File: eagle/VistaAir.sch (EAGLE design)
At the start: 11 parts

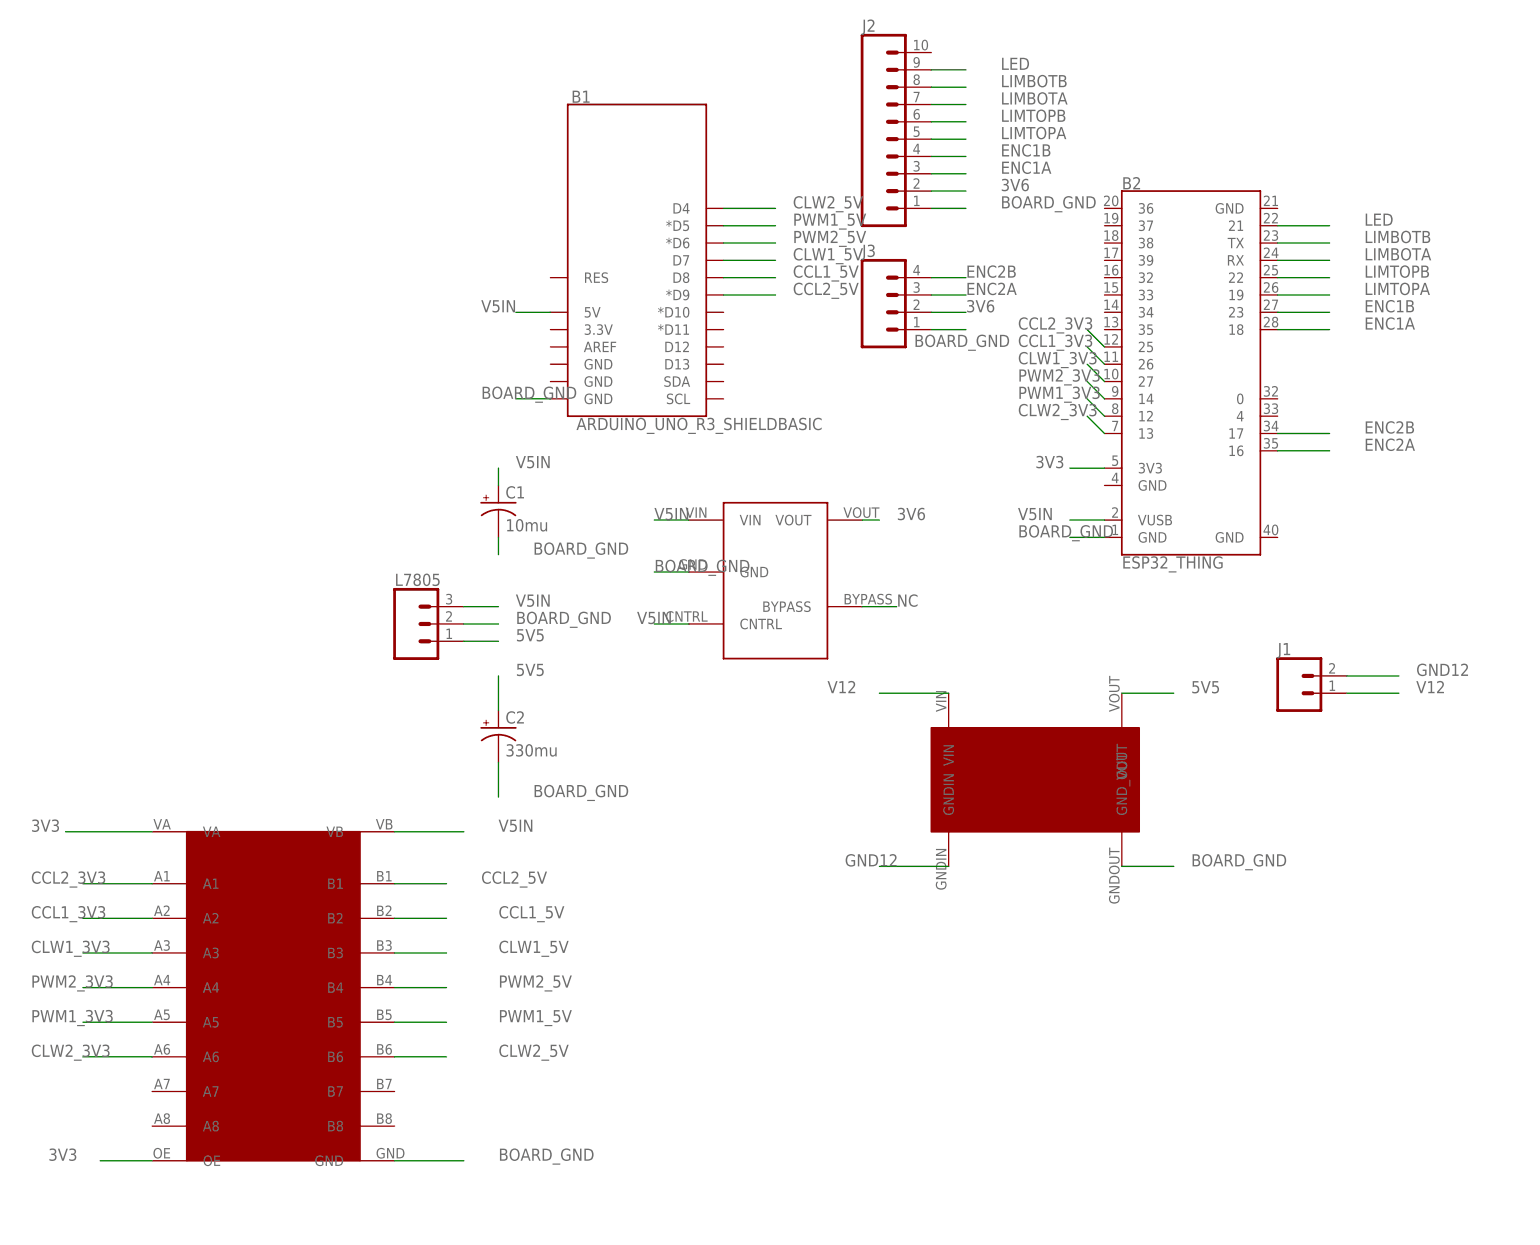
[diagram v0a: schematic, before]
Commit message: still trying to get single power board to work with logic shifter - still failing
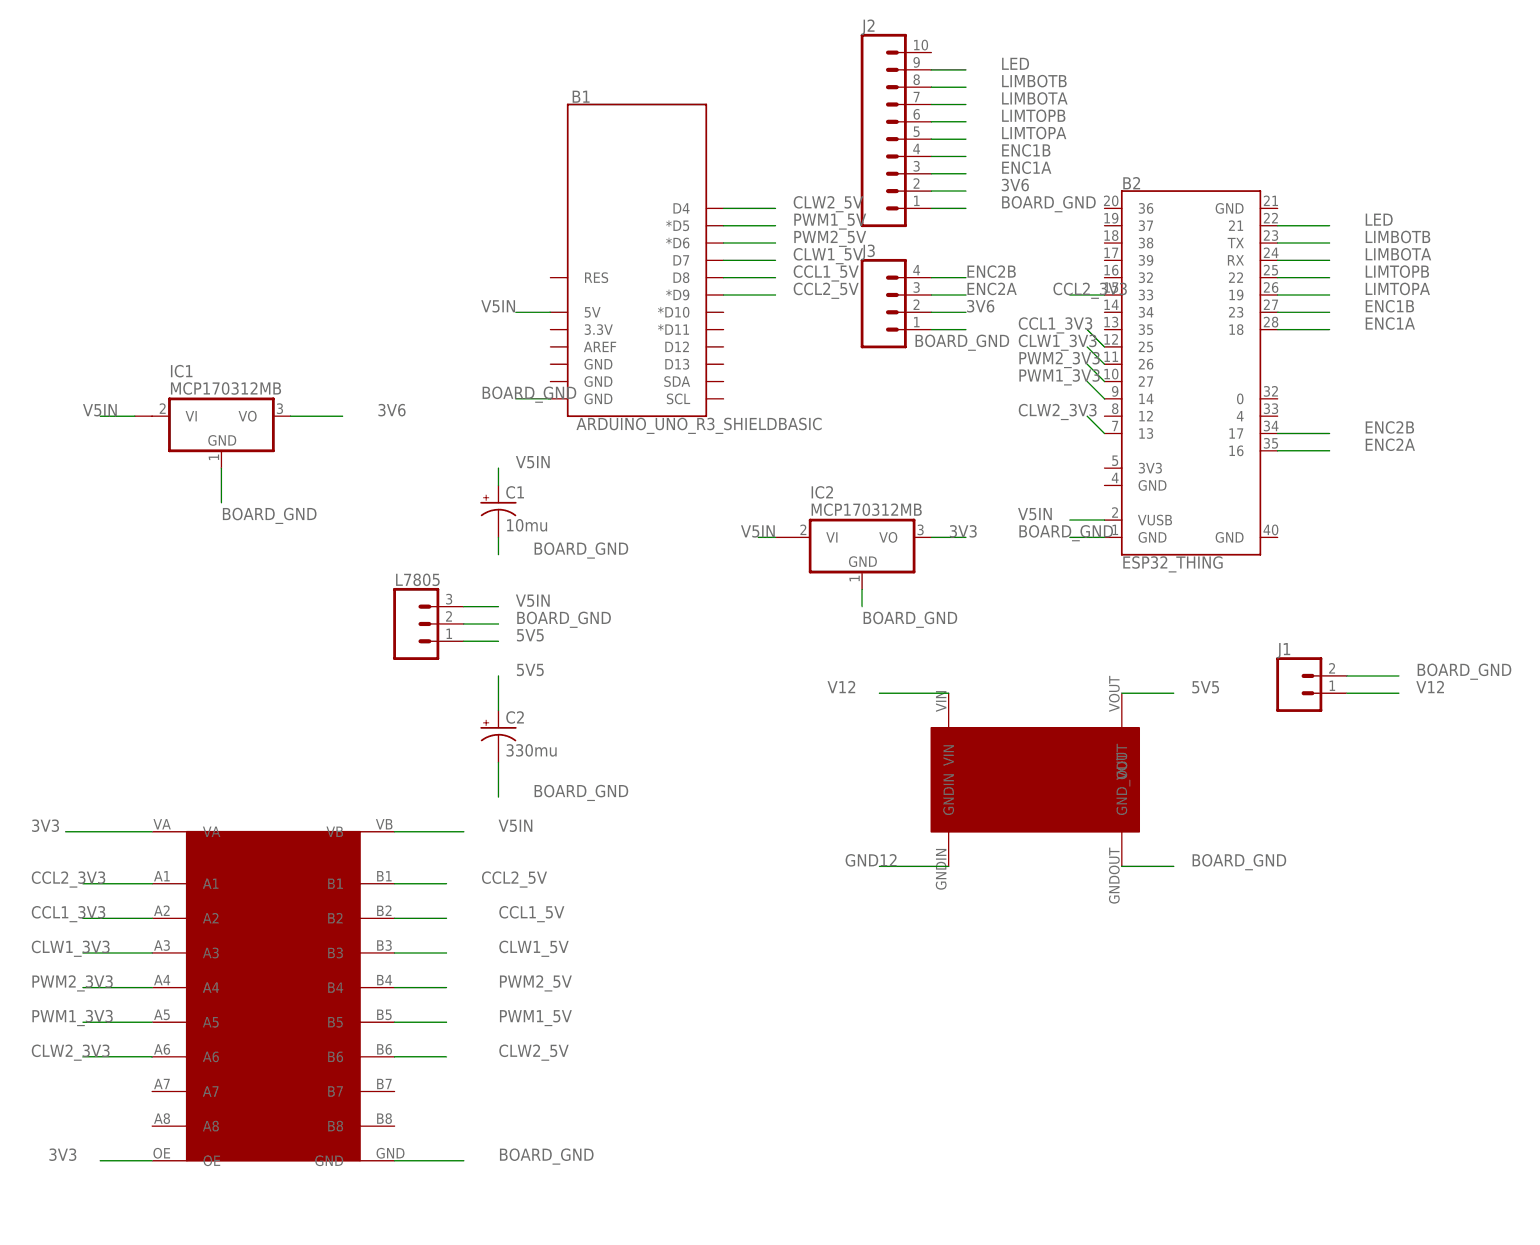
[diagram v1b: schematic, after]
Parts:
- removed U$1: LDO_REGULATOR_LP2985-N, kevins_parts:LDO_REGULATOR_LP2985-N
- added IC1, IC2: MCP170312MB, linear:MCP170312MB
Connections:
- removed net NC: U$1.BYPASS
- net 3V3: now also IC2.VO; no longer B2.3V3@5
- net 3V6: now also IC1.VO; no longer U$1.VOUT
- net BOARD_GND: now also IC1.GND, IC2.GND, J1.2; no longer U$1.GND
- net CCL1_3V3: now also B2.25; no longer B2.26
- net CCL2_3V3: now also B2.33; no longer B2.25
- net CLW1_3V3: now also B2.26; no longer B2.27
- net GND12: no longer J1.2
- net PWM1_3V3: now also B2.14; no longer B2.12
- net PWM2_3V3: now also B2.27; no longer B2.14
- net V5IN: now also IC1.VI1, IC2.VI1; no longer U$1.CNTRL, U$1.VIN
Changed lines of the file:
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@@
 <part name="C1" library="adafruit" deviceset="CPOL-US" device="TT2D5" value="10mu"/>
 <part name="U$2" library="kevins_parts" deviceset="LM2596_STEPDOWN_MODULE" device=""/>
-<part name="U$1" library="kevins_parts" deviceset="LDO_REGULATOR_LP2985-N" device=""/>
 <part name="U$3" library="kevins_parts" deviceset="8_CHANNEL_LOGIC_CONVERTER" device=""/>
+<part name="IC1" library="linear" deviceset="MCP1703*" device="MB" technology="12"/>
+<part name="IC2" library="linear" deviceset="MCP1703*" device="MB" technology="12"/>
 </parts>
 <sheets>
@@
 <instance part="C1" gate="G$1" x="25.4" y="40.64"/>
 <instance part="U$2" gate="G$1" x="99.06" y="-27.94" rot="R270"/>
-<instance part="U$1" gate="G$1" x="83.82" y="30.48"/>
 <instance part="U$3" gate="G$1" x="5.08" y="-35.56"/>
+<instance part="IC1" gate="G$1" x="-15.24" y="53.34"/>
+<instance part="IC2" gate="G$1" x="78.74" y="35.56"/>
 </instances>
 <busses>
@@
 <net name="CLW1_3V3" class="0">
 <segment>
+<pinref part="U$3" gate="G$1" pin="A3"/>
+<wire x1="-25.4" y1="-25.4" x2="-35.56" y2="-25.4" width="0.1524" layer="91"/>
+<label x="-43.18" y="-25.4" size="1.778" layer="95"/>
+</segment>
+<segment>
+<wire x1="114.3" y1="60.96" x2="111.76" y2="63.5" width="0.1524" layer="91"/>
+<label x="101.6" y="63.5" size="1.778" layer="95"/>
+<pinref part="B2" gate="G$1" pin="26"/>
+</segment>
+</net>
+<net name="PWM2_3V3" class="0">
+<segment>
+<pinref part="U$3" gate="G$1" pin="A4"/>
+<wire x1="-25.4" y1="-30.48" x2="-35.56" y2="-30.48" width="0.1524" layer="91"/>
+<label x="-43.18" y="-30.48" size="1.778" layer="95"/>
+</segment>
+<segment>
 <wire x1="114.3" y1="58.42" x2="111.76" y2="60.96" width="0.1524" layer="91"/>
 <label x="101.6" y="60.96" size="1.778" layer="95"/>
 <pinref part="B2" gate="G$1" pin="27"/>
 </segment>
-<segment>
-<pinref part="U$3" gate="G$1" pin="A3"/>
-<wire x1="-25.4" y1="-25.4" x2="-35.56" y2="-25.4" width="0.1524" layer="91"/>
-<label x="-43.18" y="-25.4" size="1.778" layer="95"/>
-</segment>
-</net>
-<net name="PWM2_3V3" class="0">
+</net>
+<net name="PWM1_3V3" class="0">
+<segment>
+<pinref part="U$3" gate="G$1" pin="A5"/>
+<wire x1="-25.4" y1="-35.56" x2="-35.56" y2="-35.56" width="0.1524" layer="91"/>
+<label x="-43.18" y="-35.56" size="1.778" layer="95"/>
+</segment>
 <segment>
 <wire x1="114.3" y1="55.88" x2="111.76" y2="58.42" width="0.1524" layer="91"/>
@@
 <pinref part="B2" gate="G$1" pin="14"/>
 </segment>
-<segment>
-<pinref part="U$3" gate="G$1" pin="A4"/>
-<wire x1="-25.4" y1="-30.48" x2="-35.56" y2="-30.48" width="0.1524" layer="91"/>
-<label x="-43.18" y="-30.48" size="1.778" layer="95"/>
-</segment>
-</net>
-<net name="PWM1_3V3" class="0">
-<segment>
-<wire x1="114.3" y1="53.34" x2="111.76" y2="55.88" width="0.1524" layer="91"/>
-<label x="101.6" y="55.88" size="1.778" layer="95"/>
-<pinref part="B2" gate="G$1" pin="12"/>
-</segment>
-<segment>
-<pinref part="U$3" gate="G$1" pin="A5"/>
-<wire x1="-25.4" y1="-35.56" x2="-35.56" y2="-35.56" width="0.1524" layer="91"/>
-<label x="-43.18" y="-35.56" size="1.778" layer="95"/>
-</segment>
 </net>
 <net name="CLW2_3V3" class="0">
@@
 <net name="CCL1_3V3" class="0">
 <segment>
-<wire x1="114.3" y1="60.96" x2="111.76" y2="63.5" width="0.1524" layer="91"/>
-<label x="101.6" y="63.5" size="1.778" layer="95"/>
-<pinref part="B2" gate="G$1" pin="26"/>
-</segment>
-<segment>
 <pinref part="U$3" gate="G$1" pin="A2"/>
 <wire x1="-25.4" y1="-20.32" x2="-35.56" y2="-20.32" width="0.1524" layer="91"/>
 <label x="-43.18" y="-20.32" size="1.778" layer="95"/>
 </segment>
-</net>
-<net name="CCL2_3V3" class="0">
 <segment>
 <wire x1="114.3" y1="63.5" x2="111.76" y2="66.04" width="0.1524" layer="91"/>
@@
 <pinref part="B2" gate="G$1" pin="25"/>
 </segment>
+</net>
+<net name="CCL2_3V3" class="0">
 <segment>
 <pinref part="U$3" gate="G$1" pin="A1"/>
@@
 <label x="-43.18" y="-15.24" size="1.778" layer="95"/>
 </segment>
+<segment>
+<pinref part="B2" gate="G$1" pin="33"/>
+<wire x1="114.3" y1="71.12" x2="109.22" y2="71.12" width="0.1524" layer="91"/>
+<label x="106.68" y="71.12" size="1.778" layer="95"/>
+</segment>
 </net>
 <net name="BOARD_GND" class="1">
@@
 </segment>
 <segment>
-<pinref part="U$1" gate="G$1" pin="GND"/>
-<wire x1="53.34" y1="30.48" x2="48.26" y2="30.48" width="0.1524" layer="91"/>
-<label x="48.26" y="30.48" size="1.778" layer="95"/>
-</segment>
-<segment>
 <pinref part="B1" gate="G$1" pin="GND@0"/>
 <wire x1="33.02" y1="55.88" x2="27.94" y2="55.88" width="0.1524" layer="91"/>
@@
 <label x="25.4" y="-55.88" size="1.778" layer="95"/>
 </segment>
+<segment>
+<pinref part="IC1" gate="G$1" pin="GND"/>
+<wire x1="-15.24" y1="45.72" x2="-15.24" y2="40.64" width="0.1524" layer="91"/>
+<label x="-15.24" y="38.1" size="1.778" layer="95"/>
+</segment>
+<segment>
+<pinref part="IC2" gate="G$1" pin="GND"/>
+<wire x1="78.74" y1="27.94" x2="78.74" y2="25.4" width="0.1524" layer="91"/>
+<label x="78.74" y="22.86" size="1.778" layer="95"/>
+</segment>
+<segment>
+<pinref part="J1" gate="G$1" pin="2"/>
+<wire x1="149.86" y1="15.24" x2="157.48" y2="15.24" width="0.1524" layer="91"/>
+<label x="160.02" y="15.24" size="1.778" layer="95"/>
+</segment>
 </net>
 <net name="ENC2B" class="0">
@@
 <net name="V5IN" class="1">
 <segment>
+<pinref part="B1" gate="G$1" pin="5V"/>
+<wire x1="33.02" y1="68.58" x2="27.94" y2="68.58" width="0.1524" layer="91"/>
+<label x="22.86" y="68.58" size="1.778" layer="95"/>
+</segment>
+<segment>
+<pinref part="C1" gate="G$1" pin="+"/>
+<wire x1="25.4" y1="43.18" x2="25.4" y2="45.72" width="0.1524" layer="91"/>
+<label x="27.94" y="45.72" size="1.778" layer="95"/>
+</segment>
+<segment>
+<pinref part="L7805" gate="J$1" pin="3"/>
+<wire x1="20.32" y1="25.4" x2="25.4" y2="25.4" width="0.1524" layer="91"/>
+<label x="27.94" y="25.4" size="1.778" layer="95"/>
+</segment>
+<segment>
+<pinref part="U$3" gate="G$1" pin="VB"/>
+<wire x1="10.16" y1="-7.62" x2="20.32" y2="-7.62" width="0.1524" layer="91"/>
+<label x="25.4" y="-7.62" size="1.778" layer="95"/>
+</segment>
+<segment>
+<pinref part="IC1" gate="G$1" pin="VI1"/>
+<wire x1="-27.94" y1="53.34" x2="-33.02" y2="53.34" width="0.1524" layer="91"/>
+<label x="-35.56" y="53.34" size="1.778" layer="95"/>
+</segment>
+<segment>
+<pinref part="IC2" gate="G$1" pin="VI1"/>
+<wire x1="66.04" y1="35.56" x2="63.5" y2="35.56" width="0.1524" layer="91"/>
+<label x="60.96" y="35.56" size="1.778" layer="95"/>
+</segment>
+<segment>
 <wire x1="114.3" y1="38.1" x2="109.22" y2="38.1" width="0.1524" layer="91"/>
 <label x="101.6" y="38.1" size="1.778" layer="95"/>
 <pinref part="B2" gate="G$1" pin="VUSB@2"/>
 </segment>
-<segment>
-<pinref part="B1" gate="G$1" pin="5V"/>
-<wire x1="33.02" y1="68.58" x2="27.94" y2="68.58" width="0.1524" layer="91"/>
-<label x="22.86" y="68.58" size="1.778" layer="95"/>
-</segment>
-<segment>
-<pinref part="C1" gate="G$1" pin="+"/>
-<wire x1="25.4" y1="43.18" x2="25.4" y2="45.72" width="0.1524" layer="91"/>
-<label x="27.94" y="45.72" size="1.778" layer="95"/>
-</segment>
-<segment>
-<pinref part="L7805" gate="J$1" pin="3"/>
-<wire x1="20.32" y1="25.4" x2="25.4" y2="25.4" width="0.1524" layer="91"/>
-<label x="27.94" y="25.4" size="1.778" layer="95"/>
-</segment>
-<segment>
-<pinref part="U$1" gate="G$1" pin="VIN"/>
-<wire x1="53.34" y1="38.1" x2="48.26" y2="38.1" width="0.1524" layer="91"/>
-<label x="48.26" y="38.1" size="1.778" layer="95"/>
-</segment>
-<segment>
-<pinref part="U$1" gate="G$1" pin="CNTRL"/>
-<wire x1="53.34" y1="22.86" x2="48.26" y2="22.86" width="0.1524" layer="91"/>
-<label x="45.72" y="22.86" size="1.778" layer="95"/>
-</segment>
-<segment>
-<pinref part="U$3" gate="G$1" pin="VB"/>
-<wire x1="10.16" y1="-7.62" x2="20.32" y2="-7.62" width="0.1524" layer="91"/>
-<label x="25.4" y="-7.62" size="1.778" layer="95"/>
-</segment>
 </net>
 <net name="LIMTOPA" class="0">
@@
 <net name="GND12" class="1">
 <segment>
-<pinref part="J1" gate="G$1" pin="2"/>
-<wire x1="149.86" y1="15.24" x2="157.48" y2="15.24" width="0.1524" layer="91"/>
-<label x="160.02" y="15.24" size="1.778" layer="95"/>
-</segment>
-<segment>
 <pinref part="U$2" gate="G$1" pin="GNDIN"/>
 <wire x1="91.44" y1="-12.7" x2="81.28" y2="-12.7" width="0.1524" layer="91"/>
@@
 </segment>
 <segment>
-<pinref part="U$1" gate="G$1" pin="VOUT"/>
-<wire x1="78.74" y1="38.1" x2="81.28" y2="38.1" width="0.1524" layer="91"/>
-<label x="83.82" y="38.1" size="1.778" layer="95"/>
+<pinref part="IC1" gate="G$1" pin="VO"/>
+<wire x1="-5.08" y1="53.34" x2="2.54" y2="53.34" width="0.1524" layer="91"/>
+<label x="7.62" y="53.34" size="1.778" layer="95"/>
 </segment>
 </net>
@@
 </segment>
 </net>
-<net name="NC" class="0">
-<segment>
-<pinref part="U$1" gate="G$1" pin="BYPASS"/>
-<wire x1="78.74" y1="25.4" x2="83.82" y2="25.4" width="0.1524" layer="91"/>
-<label x="83.82" y="25.4" size="1.778" layer="95"/>
-</segment>
-</net>
 <net name="3V3" class="0">
-<segment>
-<pinref part="B2" gate="G$1" pin="3V3@5"/>
-<wire x1="114.3" y1="45.72" x2="109.22" y2="45.72" width="0.1524" layer="91"/>
-<label x="104.14" y="45.72" size="1.778" layer="95"/>
-</segment>
 <segment>
 <pinref part="U$3" gate="G$1" pin="VA"/>
@@
 <label x="-40.64" y="-55.88" size="1.778" layer="95"/>
 </segment>
-</net>
+<segment>
+<pinref part="IC2" gate="G$1" pin="VO"/>
+<wire x1="88.9" y1="35.56" x2="93.98" y2="35.56" width="0.1524" layer="91"/>
+<label x="91.44" y="35.56" size="1.778" layer="95"/>
+</segment>
+</net>

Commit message: barrel jack for board, fix pin numbers for arduino motor test and simplify board - diodes seem to be surplus to requirements. Logic shifting issue is something else
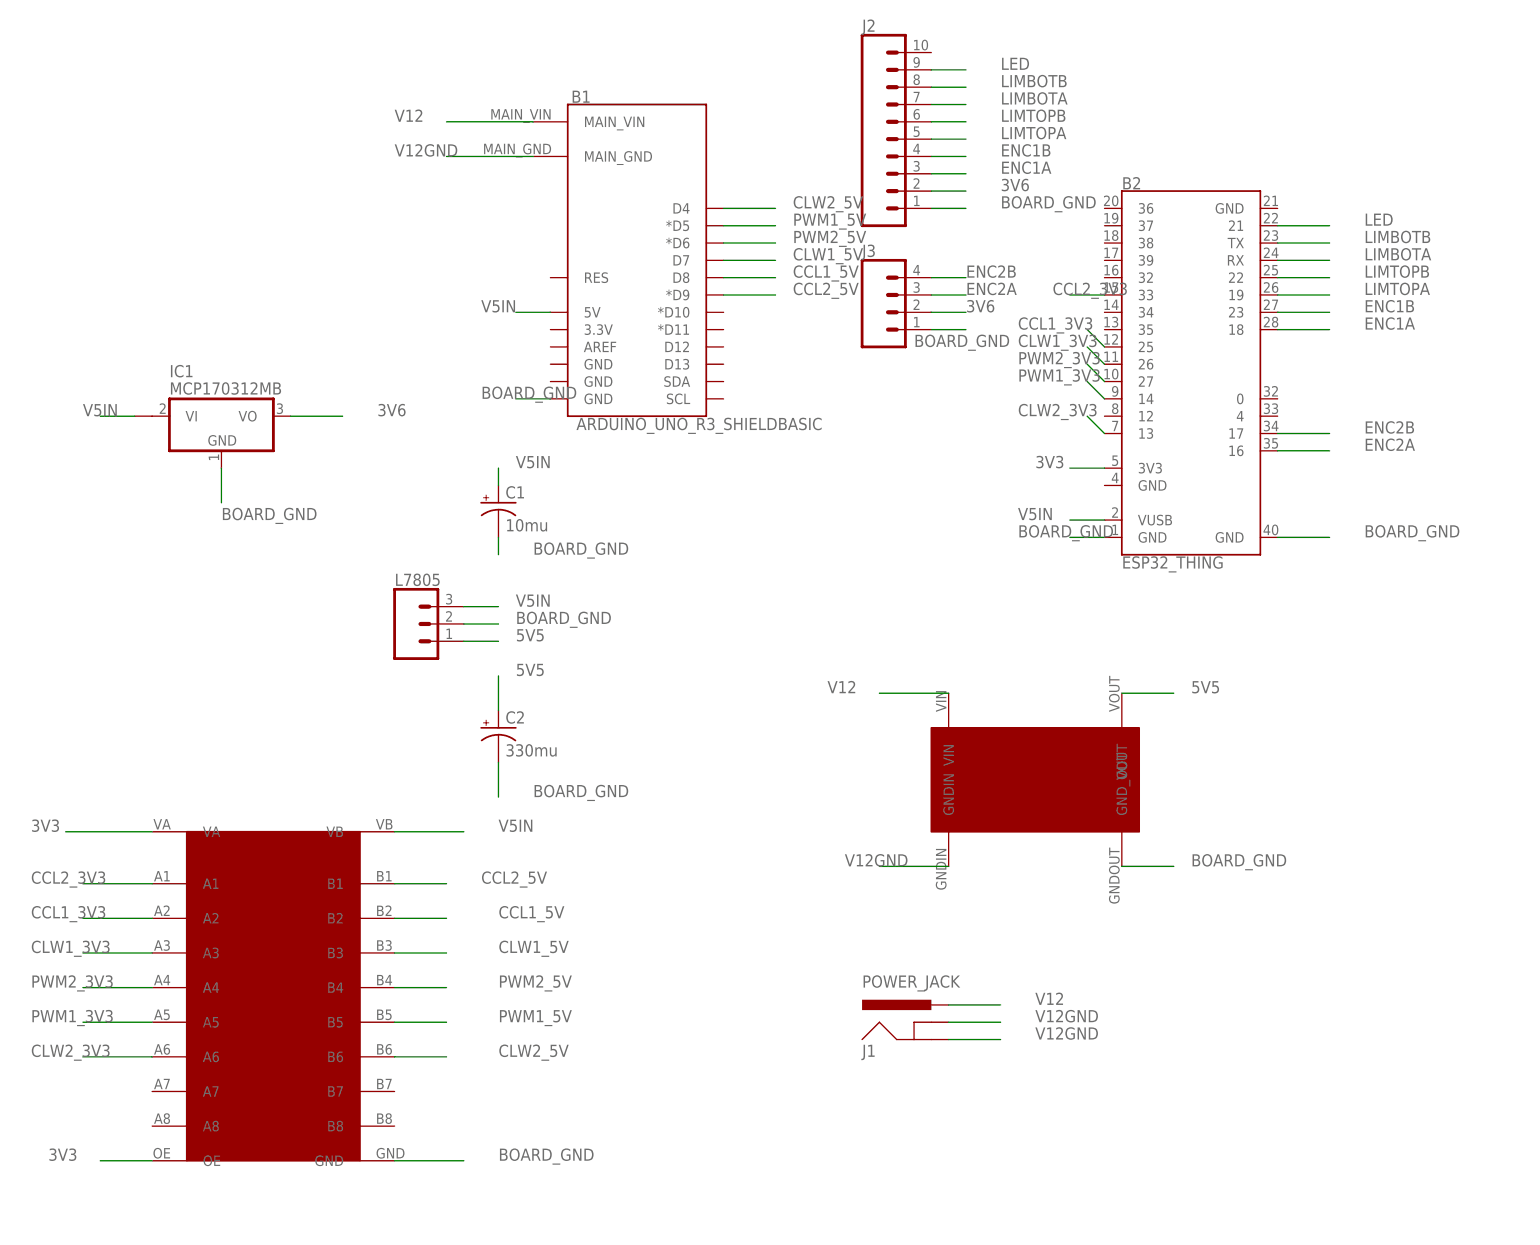
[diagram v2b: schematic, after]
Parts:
- removed IC2: MCP170312MB, linear:MCP170312MB
- J1: value (none) -> POWER_JACK; device SparkFun-Connectors:CONN_02PTH4 -> SparkFun-Connectors:POWER_JACK
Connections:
- removed net GND12: U$2.GNDIN
- new net V12GND: B1.MAIN_GND, J1.GND, J1.GNDBREAK, U$2.GNDIN
- net 3V3: now also B2.3V3@5; no longer IC2.VO
- net BOARD_GND: now also B2.GND@40; no longer IC2.GND, J1.2
- net V12: now also B1.MAIN_VIN, J1.PWR; no longer J1.1
- net V5IN: no longer IC2.VI1
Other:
- moved on the sheet: J1
